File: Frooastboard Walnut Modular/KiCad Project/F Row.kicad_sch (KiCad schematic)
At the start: 61 parts

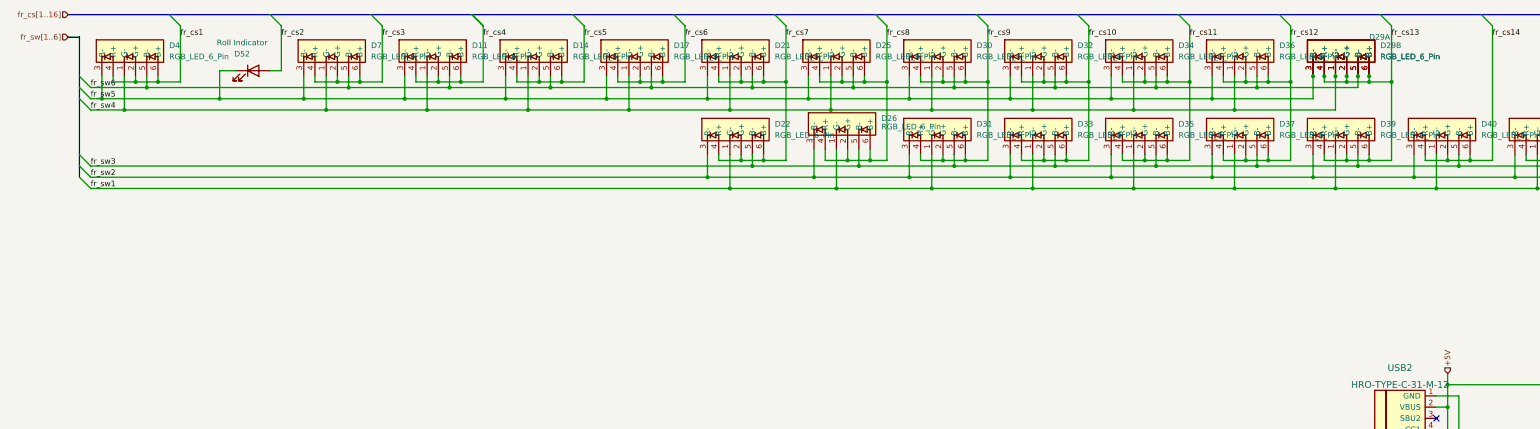
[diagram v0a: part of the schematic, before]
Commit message: update reference multi leds
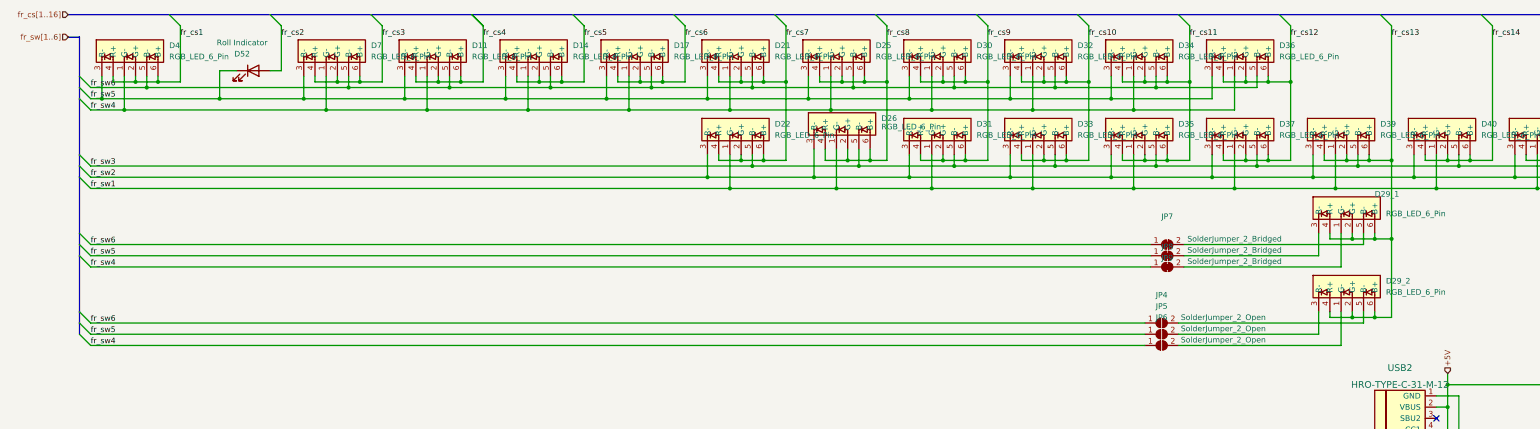
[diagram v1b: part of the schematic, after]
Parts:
- added JP4, JP5, JP6: SolderJumper_2_Open, Jumper:SolderJumper-2_P1.3mm_Open_RoundedPad1.0x1.5mm, symbol Jumper:SolderJumper_2_Open
- added JP7, JP8, JP9: SolderJumper_2_Bridged, Jumper:SolderJumper-2_P1.3mm_Bridged_RoundedPad1.0x1.5mm, symbol Jumper:SolderJumper_2_Bridged
- renumbered D29A to D29_1, D29B to D29_2
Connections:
- net fr_sw4: now also JP6.1 (A), JP9.1 (A); no longer D29_1.1 (G-), D29_2.1 (G-)
- net fr_sw5: now also JP5.1 (A), JP8.1 (A); no longer D29_1.3 (R-), D29_2.3 (R-)
- net fr_sw6: now also JP4.1 (A), JP7.1 (A); no longer D29_1.5 (B-), D29_2.5 (B-)
- new net: D29_2.3 (R-), JP5.2 (B)
- new net: D29_1.1 (G-), JP9.2 (B)
- new net: D29_1.3 (R-), JP8.2 (B)
- new net: D29_1.5 (B-), JP7.2 (B)
- new net: D29_2.1 (G-), JP6.2 (B)
- new net: D29_2.5 (B-), JP4.2 (B)
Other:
- moved on the sheet: D29_1, D29_2

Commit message: idk some updates
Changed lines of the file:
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@@
-    (effects (font (size 1.27 1.27)) (justify left bottom))
-  )
-  (label "D+" (at 345.44 120.65 0) (fields_autoplaced)
     (effects (font (size 1.27 1.27)) (justify left bottom))
   )
@@
     (effects (font (size 1.27 1.27)) (justify left bottom))
   )
-  (label "D-" (at 345.44 118.11 0) (fields_autoplaced)
-    (effects (font (size 1.27 1.27)) (justify left bottom))
-  )

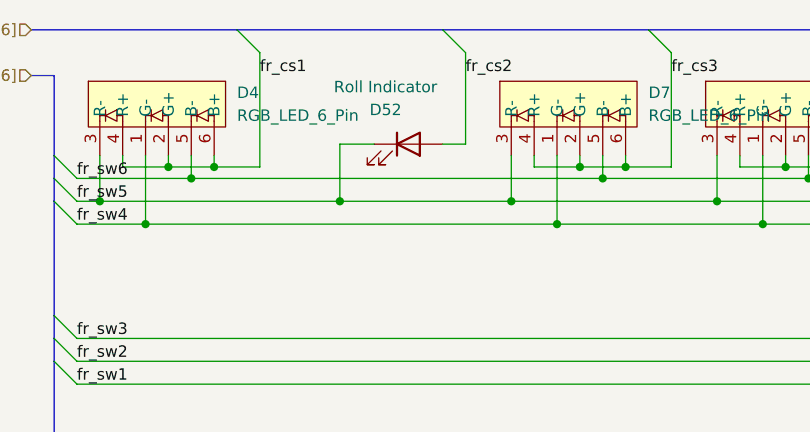
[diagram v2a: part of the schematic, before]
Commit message: update leds and diodes
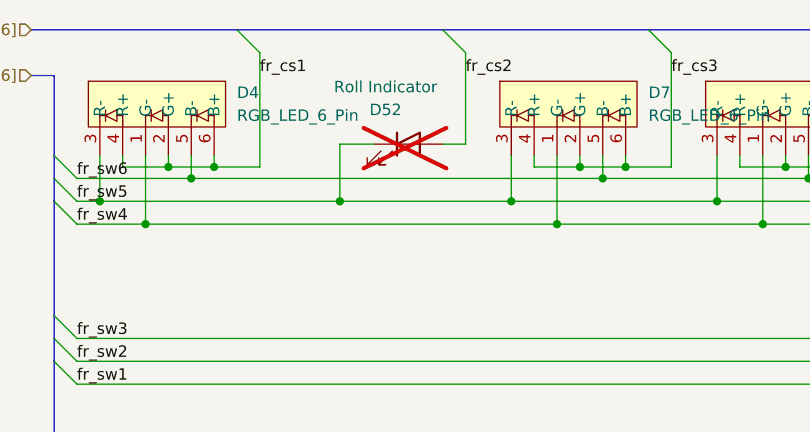
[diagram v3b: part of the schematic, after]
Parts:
- D52: now not fitted; now left out of the parts list
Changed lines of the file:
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@@
   )
   (symbol (lib_id "Device:LED") (at 68.58 34.29 0) (unit 1)
-    (in_bom yes) (on_board yes) (dnp no)
+    (in_bom no) (on_board no) (dnp yes)
     (property "Reference" "D52" (at 66.04 30.48 0)
       (effects (font (size 1.27 1.27)))

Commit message: some stuff
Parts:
- MX147: value MX-LED -> Scroll Lock
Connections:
- net fr_col0: now also MX9.1 (COL); no longer MX2.1 (COL)
- net fr_col1: now also MX10.1 (COL), MX2.1 (COL); no longer MX3.1 (COL), MX4.1 (COL)
- net fr_col2: now also MX11.1 (COL), MX3.1 (COL); no longer MX5.1 (COL), MX6.1 (COL)
- net fr_col3: now also MX12.1 (COL), MX4.1 (COL); no longer MX7.1 (COL), MX8.1 (COL)
- net fr_col4: now also MX13.1 (COL), MX5.1 (COL); no longer MX10.1 (COL), MX9.1 (COL)
- net fr_col5: now also MX14.1 (COL), MX6.1 (COL); no longer MX11.1 (COL), MX12.1 (COL)
- net fr_col6: now also MX147.1 (COL), MX7.1 (COL); no longer MX13.1 (COL), MX14.1 (COL)
- net fr_col7: now also MX8.1 (COL); no longer MX147.1 (COL)
- net fr_row10: now also D10.1 (K), D13.1 (K), D16.1 (K), D8.1 (K); no longer D18.1 (K), D20.1 (K), D24.1 (K), D28.1 (K)
- net fr_row11: now also D18.1 (K), D20.1 (K), D24.1 (K), D28.1 (K); no longer D10.1 (K), D13.1 (K), D16.1 (K), D8.1 (K)
- net fr_dn renamed fr_d-
- net fr_dp renamed fr_d+
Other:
- moved on the sheet: D10, D12, D13, D15, D16, D18, D19, D20, D23, D24, D27, D28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
